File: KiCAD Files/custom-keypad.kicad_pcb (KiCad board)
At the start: 2 copper layers, 67.8 x 65.6 mm, 50 parts, among them IC1 AZ1117IH-3.3TRG1, IC2 USBLC6-2SC6, J1 UJ32-C-H-G-H2-SMT-TR, J2 EN11-HSM1BF20, J3 61300511121, SW1 SW_Push, SW2 SW_Push, SW3 SW_Push, SW4 SW_Push, SW8 SW_Push, SW9 SW_Push, U1 STM32H7A3RGTx, Y2 XRCGB25M000FAN00R0

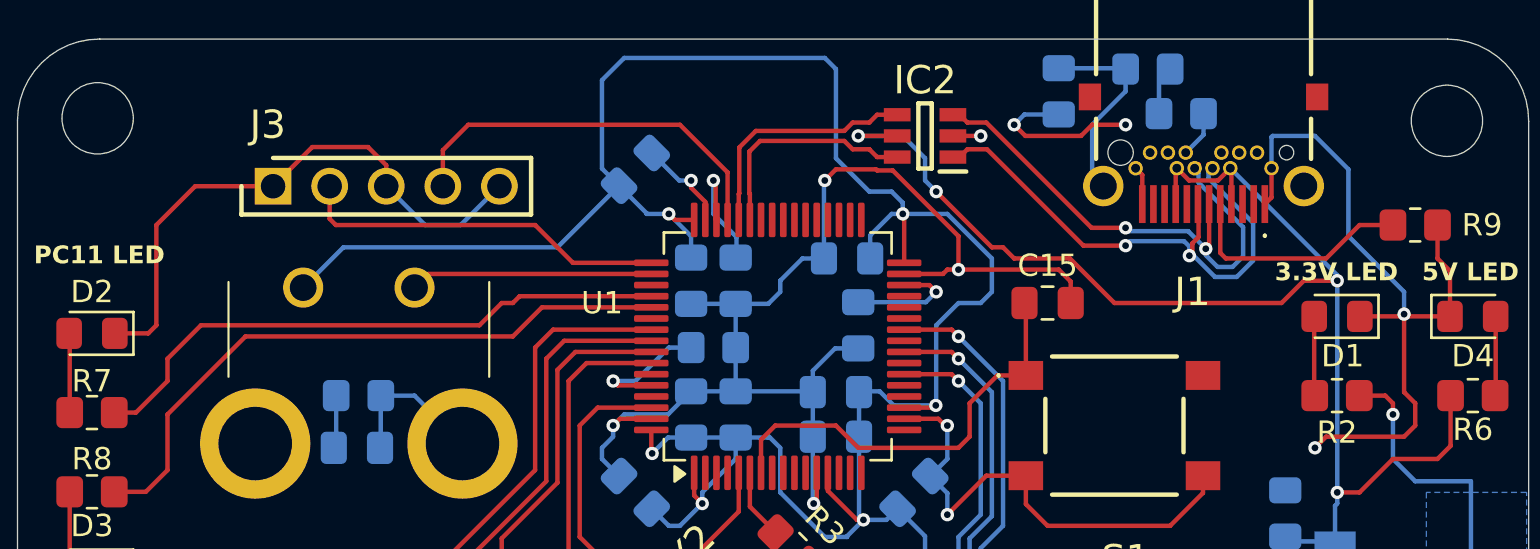
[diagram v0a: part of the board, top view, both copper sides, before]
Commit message: tweaked 3d model + added drill files for jlc
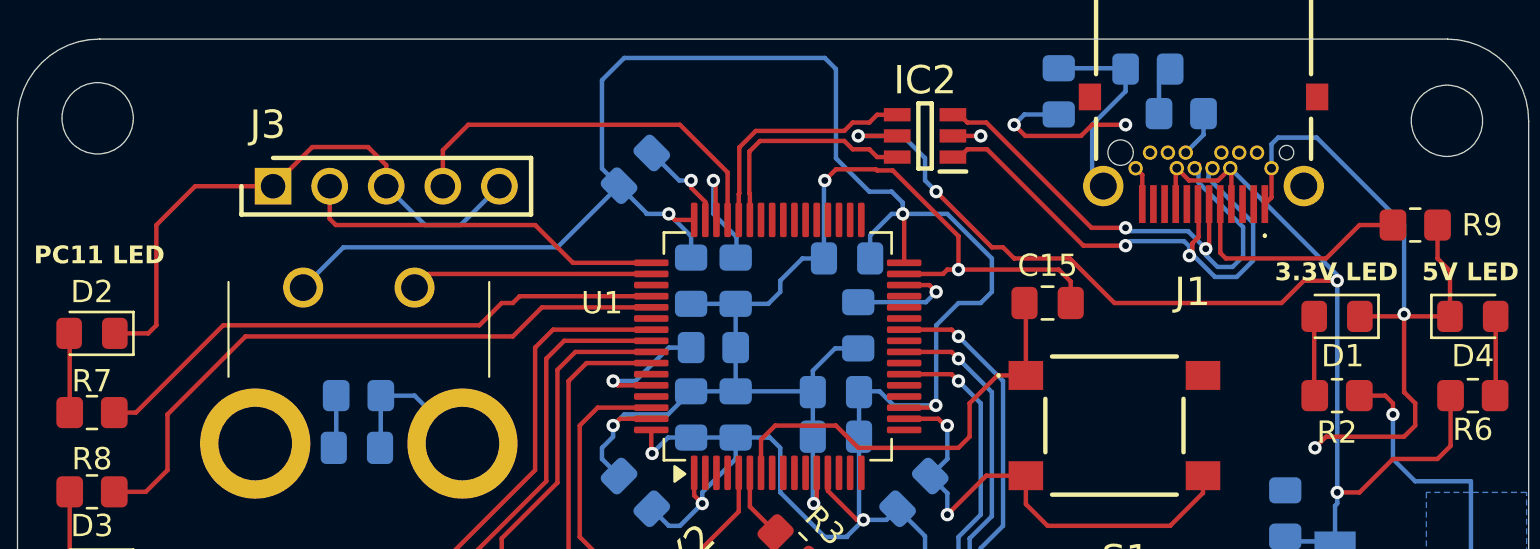
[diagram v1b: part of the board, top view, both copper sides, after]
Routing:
- net PC11/Debug PC11: track 26.9 -> 26.3 mm
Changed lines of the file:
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@@
 			(plot_on_all_layers_selection 0x0000000_00000000)
 			(disableapertmacros no)
-			(usegerberextensions no)
-			(usegerberattributes yes)
-			(usegerberadvancedattributes yes)
+			(usegerberextensions yes)
+			(usegerberattributes no)
+			(usegerberadvancedattributes no)
 			(creategerberjobfile yes)
 			(dashed_line_dash_ratio 12.000000)
@@
 			(svgprecision 4)
 			(plotframeref no)
-			(viasonmask no)
+			(viasonmask yes)
 			(mode 1)
 			(useauxorigin no)
@@
 			(psa4output no)
 			(plotreference yes)
-			(plotvalue yes)
+			(plotvalue no)
 			(plotfptext yes)
 			(plotinvisibletext no)
 			(sketchpadsonfab no)
-			(subtractmaskfromsilk no)
+			(subtractmaskfromsilk yes)
 			(outputformat 1)
 			(mirror no)
-			(drillshape 1)
+			(drillshape 0)
 			(scaleselection 1)
-			(outputdirectory "")
+			(outputdirectory "C:/Users/Jay62/570proj/custom-keypad/KiCAD Files/Gerber Files/")
 		)
 	)
@@
 			)
 		)
-		(property "Footprint" "EN11HSM1BF20"
+		(property "Footprint" "CustomFootprints:EN11HSM1BF20"
 			(at 0 0 0)
 			(layer "F.Fab")
@@
 			(layer "F.Fab")
 		)
+		(fp_text user "${REFERENCE}"
+			(at 2.5 -6.35 0)
+			(layer "F.Fab")
+			(effects
+				(font
+					(size 1.27 1.27)
+					(thickness 0.254)
+				)
+			)
+		)
 		(pad "A1" thru_hole circle
 			(at 0 0)
@@
 			(pintype "passive")
 		)
-		(model "EN11-HSM1BF20.stp"
-			(offset
-				(xyz 0 0 0)
-			)
-			(scale
-				(xyz 1 1 1)
-			)
-			(rotate
-				(xyz 0 0 0)
-			)
-		)
 		(model "${KIPRJMOD}/3D Models/EN11-HSM1BF20.stp"
 			(offset
-				(xyz 0 0 0)
+				(xyz 2.5 7.5 6.2)
 			)
 			(scale
@@
 			)
 			(rotate
-				(xyz 0 0 0)
+				(xyz -90 0 0)
 			)
 		)
@@
 	)
 	(segment
+		(start 109.575 30.075)
+		(end 113.5 34)
+		(width 0.2)
+		(layer "B.Cu")
+		(net 1)
+	)
+	(segment
 		(start 84.9625 37.5375)
 		(end 85.5 37)
@@
 	)
 	(segment
+		(start 107.55 30.372)
+		(end 107.847 30.075)
+		(width 0.2)
+		(layer "B.Cu")
+		(net 1)
+	)
+	(segment
 		(start 80.967246 32)
 		(end 81.5 32)
@@
 	)
 	(segment
-		(start 111 31.5)
-		(end 109.5 30)
+		(start 113.5 34)
+		(end 113.5 38)
 		(width 0.2)
 		(layer "B.Cu")
@@
 	)
 	(segment
-		(start 107.55 30.05)
-		(end 107.6 30)
+		(start 107.55 31.45)
+		(end 107.55 30.372)
 		(width 0.2)
 		(layer "B.Cu")
@@
 	)
 	(segment
+		(start 107.847 30.075)
+		(end 109.575 30.075)
+		(width 0.2)
+		(layer "B.Cu")
+		(net 1)
+	)
+	(segment
 		(start 92.233623 45.266377)
 		(end 93 44.5)
@@
 	)
 	(segment
-		(start 111 34.5)
-		(end 111 31.5)
-		(width 0.2)
-		(layer "B.Cu")
-		(net 1)
-	)
-	(segment
 		(start 78 43)
 		(end 78.5 42.5)
@@
 	)
 	(segment
-		(start 113.5 38)
-		(end 113.5 37)
-		(width 0.2)
-		(layer "B.Cu")
-		(net 1)
-	)
-	(segment
 		(start 83.5 41.4625)
 		(end 86.925 41.4625)
@@
 	)
 	(segment
-		(start 107.55 30.05)
-		(end 107.55 31.45)
-		(width 0.2)
-		(layer "B.Cu")
-		(net 1)
-	)
-	(segment
 		(start 86.9625 46.4625)
 		(end 87 46.5)
@@
 	)
 	(segment
-		(start 113.5 37)
-		(end 111 34.5)
-		(width 0.2)
-		(layer "B.Cu")
-		(net 1)
-	)
-	(segment
 		(start 87.9625 39.5375)
 		(end 89 39.5375)
@@
 	)
 	(segment
-		(start 107.6 30)
-		(end 109.5 30)
-		(width 0.2)
-		(layer "B.Cu")
-		(net 1)
-	)
-	(segment
 		(start 106.742 77.724)
 		(end 87.842 77.724)
@@
 	)
 	(segment
-		(start 73.5 37.5)
-		(end 73.805 37.195)
+		(start 73.805 37.195)
+		(end 79.713 37.195)
 		(width 0.2)
 		(layer "F.Cu")
@@
 	(segment
 		(start 56.582 42.418)
-		(end 58 41)
-		(width 0.2)
-		(layer "F.Cu")
-		(net 77)
-	)
-	(segment
-		(start 55.61 42.418)
-		(end 56.582 42.418)
-		(width 0.2)
-		(layer "F.Cu")
-		(net 77)
-	)
-	(segment
-		(start 72 38.5)
-		(end 73 37.5)
+		(end 60.5 38.5)
 		(width 0.2)
 		(layer "F.Cu")
@@
 	)
 	(segment
-		(start 58 41)
-		(end 58 40)
+		(start 73.5 37.5)
+		(end 73.805 37.195)
 		(width 0.2)
 		(layer "F.Cu")
@@
 	)
 	(segment
-		(start 73 37.5)
-		(end 73.5 37.5)
+		(start 60.5 38.5)
+		(end 72 38.5)
 		(width 0.2)
 		(layer "F.Cu")
@@
 	)
 	(segment
-		(start 59.5 38.5)
-		(end 72 38.5)
+		(start 55.61 42.418)
+		(end 56.582 42.418)
 		(width 0.2)
 		(layer "F.Cu")
@@
 	)
 	(segment
-		(start 58 40)
-		(end 59.5 38.5)
+		(start 73 37.5)
+		(end 73.5 37.5)
 		(width 0.2)
 		(layer "F.Cu")
@@
 	)
 	(segment
-		(start 73.805 37.195)
-		(end 79.713 37.195)
+		(start 72 38.5)
+		(end 73 37.5)
 		(width 0.2)
 		(layer "F.Cu")
